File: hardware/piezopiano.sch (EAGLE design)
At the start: 82 parts, among them J1 CON2, J4 JST-PH-2-SMT-SE, Q1 DMN3404L, Q2 DMN3404L, Q3 DMN3404L, Q4 DMN3404L, Q5 DMN3404L, Q6 DMN3404L, Q7 DMN3404L, Q8 DMN3404L, U1 ATMEGA4809, U2 CH340E_MSOP10, U3 TP4333

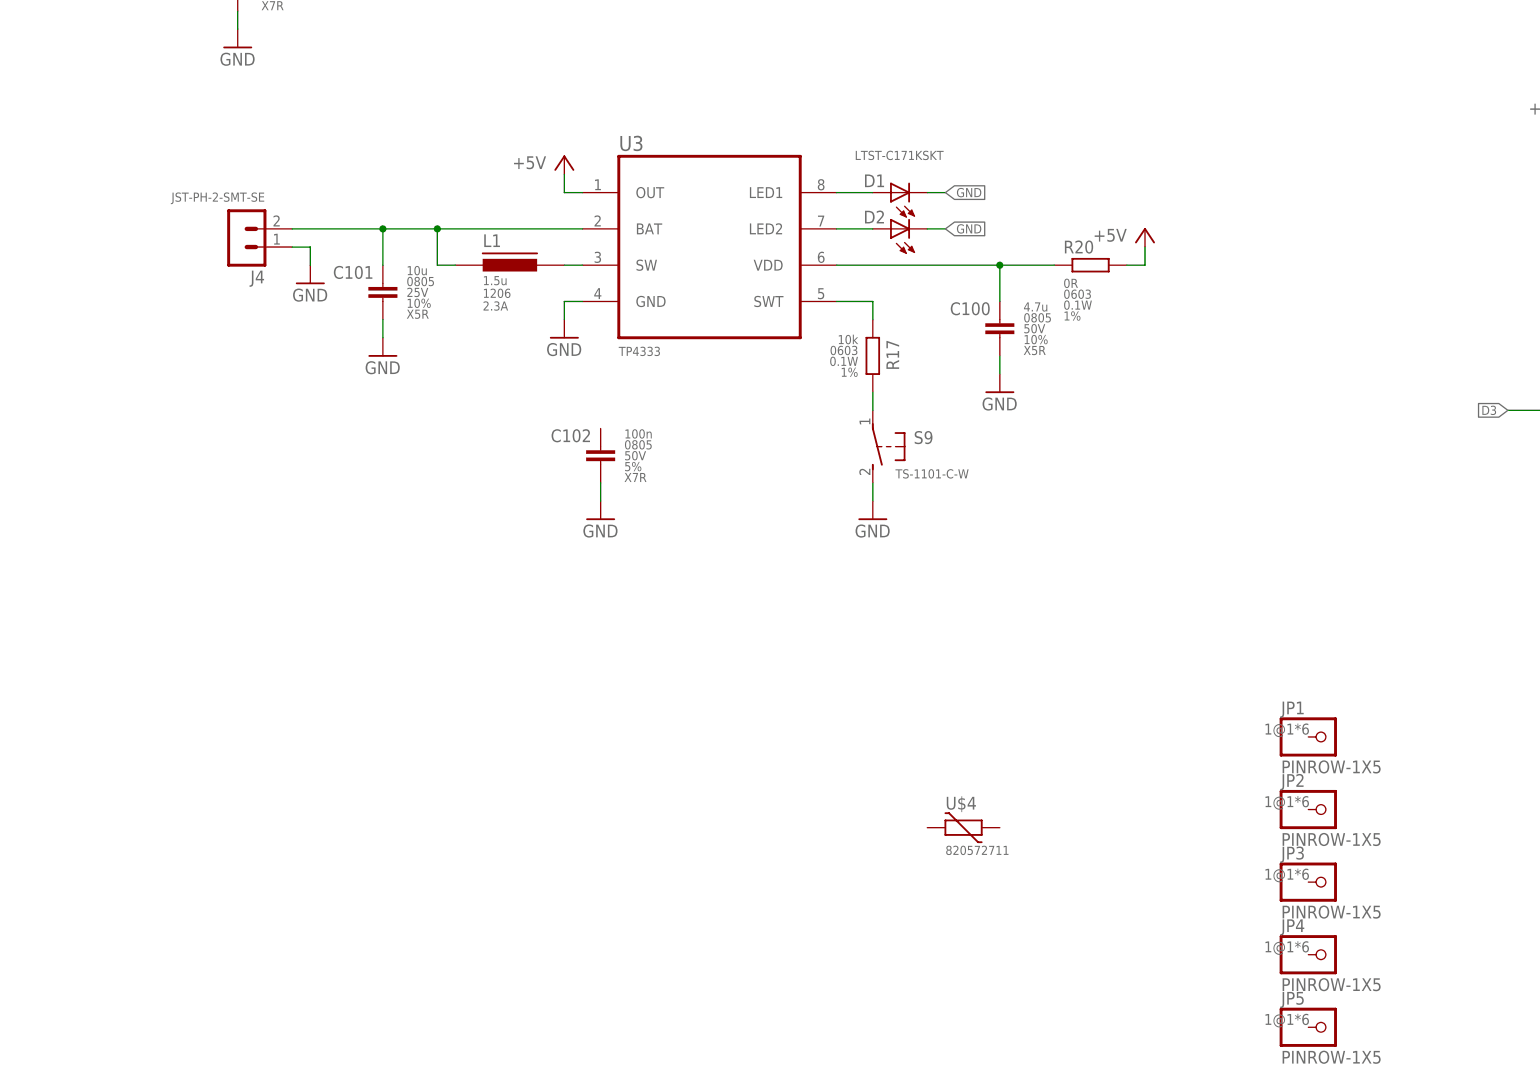
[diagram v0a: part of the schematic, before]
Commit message: Created different branch for battery support, deleted battery parts
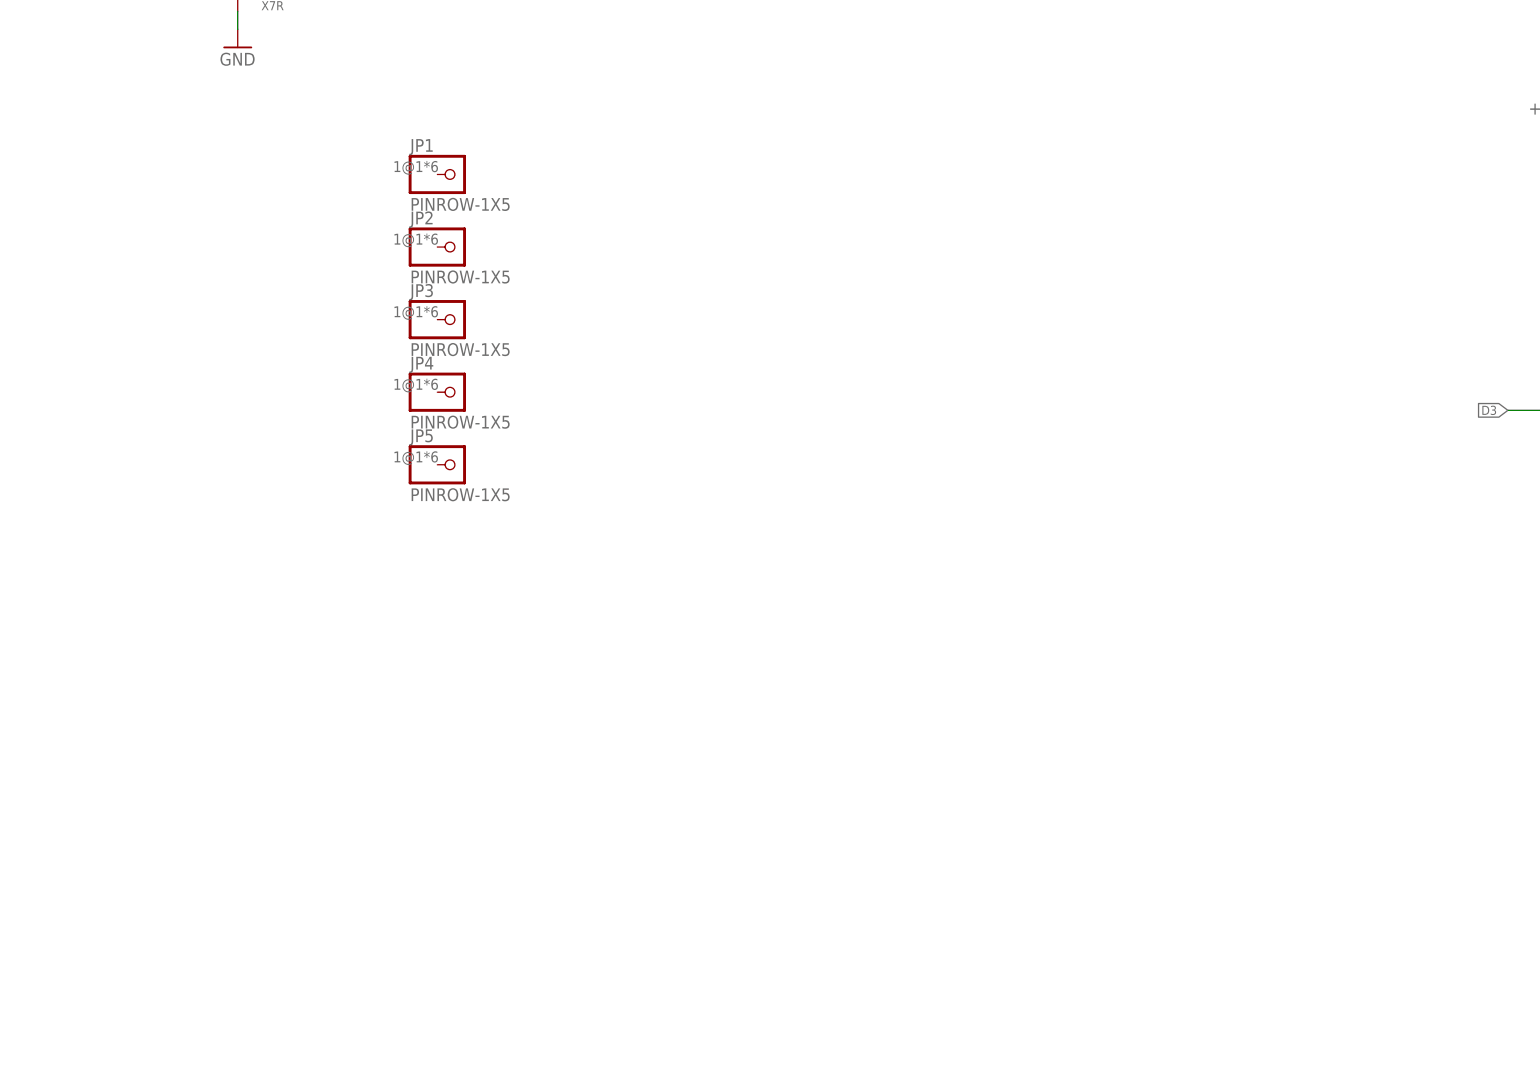
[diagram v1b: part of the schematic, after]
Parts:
- removed C100: 4.7u, zaan-Capacitors:4.7UF-0805-50V-10%
- removed C101: 10u, zaan-Capacitors:10UF-0805-25V-10%
- removed C102: 100n, zaan-Capacitors:100NF-0805-50V-5%
- removed D1, D2: LTST-C171KSKT, zaan-Optoelectronics:LTST-C171KSKT
- removed J4: JST-PH-2-SMT-SE, zaan-Connectors:JST-PH-2-SMT-SE
- removed L1: 1.5u, zaan-Inductors:WE-LQS-L3015-1.5U
- removed R17: 10k, zaan-Resistors:10KOHM-0603-1/10W-1%
- removed R20: 0R, zaan-Resistors:0OHM-0603-1/10W-1%
- removed S9: TS-1101-C-W, zaan-Electromechanical:TS-1101-C-W
- removed U$4: 820572711, zaan-No-Category:820572711
- removed U3: TP4333, zaan-IC-Power:TP4333
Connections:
- removed net N$17: C100.1, R20.1, U3.VDD
- removed net N$21: C101.1, J4.2, L1.1, U3.BAT
- removed net N$22: L1.2, U3.SW
- removed net N$23: R17.1, U3.SWT
- removed net N$24: R17.2, S9.P
- removed net N$25: D1.A, U3.LED1
- removed net N$26: D2.A, U3.LED2
- net +5V: no longer R20.2, U3.OUT
- net GND: no longer C100.2, C101.2, C102.2, D1.C, D2.C, J4.1, S9.S, U3.GND
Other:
- moved on the sheet: JP1, JP2, JP3, JP4, JP5

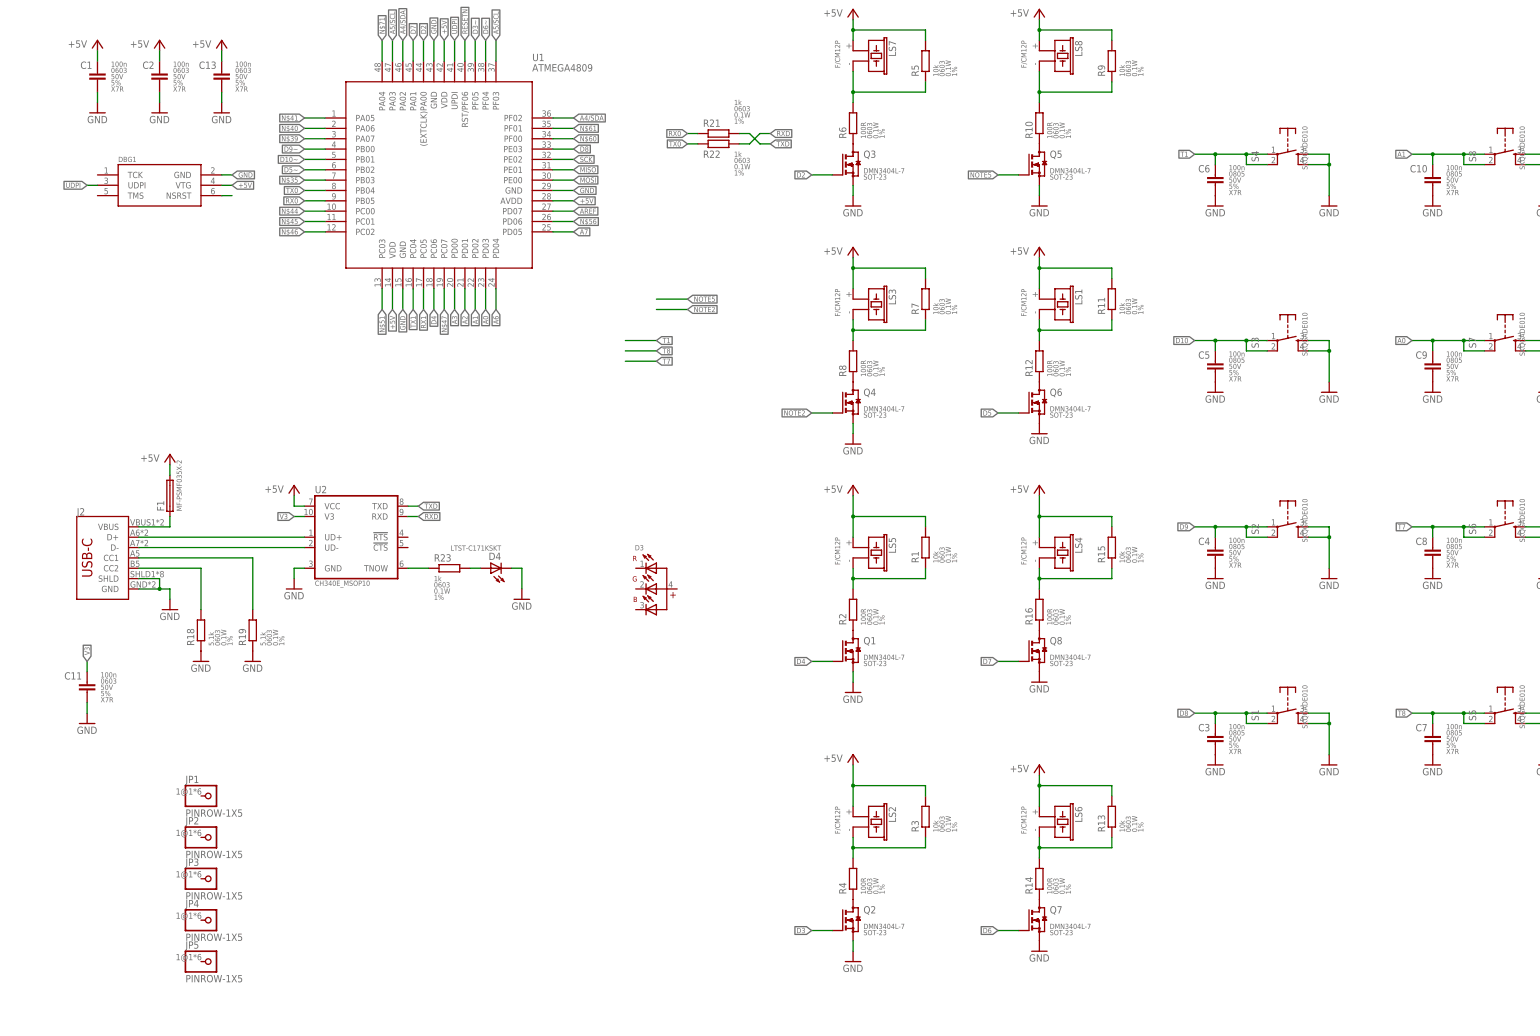
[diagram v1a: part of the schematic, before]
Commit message: Added QWIIC connector
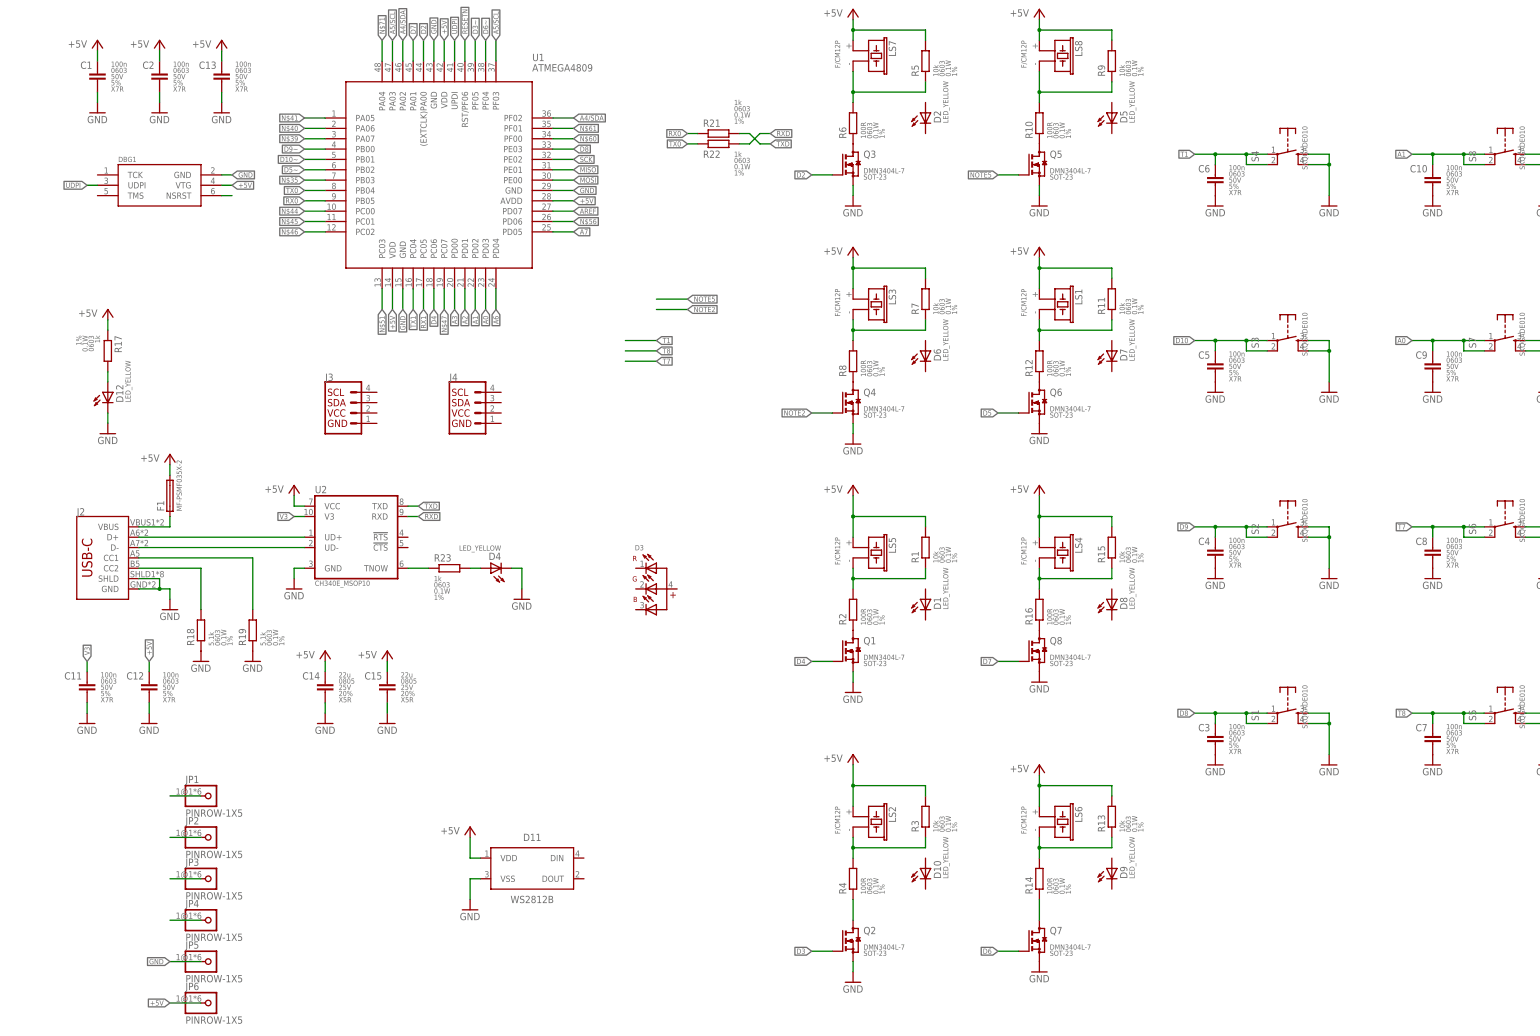
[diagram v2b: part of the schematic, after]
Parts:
- added C12: 100n, zaan-Capacitors:100NF-0603-50V-5%
- added C14, C15: 22u, zaan-Capacitors:22UF-0805-25V-20%
- added D1, D10, D12, D2, D5, D6, D7, D8, D9: LED_YELLOW, zaan-Optoelectronics:CHIP-FLAT-Y_0603-0.55MM
- added D11: WS2812B, zaan-Optoelectronics:WS2812B
- added J3, J4: (no value), zaan-Connectors:QWIIC_CONNECTORJS-1MM
- added JP6: PINROW-1X5, zaan-No-Category:PINROW-1X5
- added R17: 1k, zaan-Resistors:1KOHM-0603-1/10W-1%
- C10, C3, C4, C5, C6, C7, C8, C9: device zaan-Capacitors:100NF-0805-50V-5% -> zaan-Capacitors:100NF-0603-50V-5%
- D4: value LTST-C171KSKT -> LED_YELLOW; device zaan-Optoelectronics:LTST-C171KSKT -> zaan-Optoelectronics:CHIP-FLAT-Y_0603-0.55MM
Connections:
- new net N$22: JP4.1
- new net N$23: JP3.1
- new net N$24: JP2.1
- new net N$25: JP1.1
- new net N$8: D12.A, R17.2
- net +5V: now also C12.1, C14.1, C15.1, D11.VDD, JP6.1, R17.1
- net GND: now also C12.2, C14.2, C15.2, D11.VSS, D12.C, JP5.1
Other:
- moved on the sheet: Q2, Q7

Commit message: Routing and Placement changes
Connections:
- net N$22 renamed EXT_PH_04
- net N$23 renamed EXT_PH_03
- net N$24 renamed EXT_PH_02
- net N$25 renamed EXT_PH_01
- net N$35 renamed PB03
- net N$39 renamed PA07
- net N$40 renamed PA06
- net N$41 renamed PA05
- net N$44 renamed PC00
- net N$45 renamed PC01
- net N$46 renamed PC02
- net N$47 renamed PC07
- net N$51 renamed PC03
- net N$56 renamed PD06
- net N$60 renamed PF00
- net N$61 renamed PF01
- removed net D10: C5.1, S3.P, S3.P@1
- removed net N$28: DBG1.NSRST
- removed net N$71: U1.PA04
- removed net T1: C6.1, S4.P, S4.P@1
- removed net T8: C7.1, S5.P, S5.P@1
- new net PA04: C7.1, S5.P, S5.P@1, U1.PA04
- new net PF02: U1.PF02
- new net PF03: U1.PF03
- new net X: Q3.G
- new net Y: Q8.G
- net +5V: now also J3.VCC, J4.VCC
- net A4/SDA: now also J3.SDA, J4.SDA; no longer U1.PF02
- net A5/SCL: now also J3.SCL, J4.SCL; no longer U1.PF03
- net D2: now also C5.1, S3.P, S3.P@1; no longer Q3.G
- net D7: now also C6.1, S4.P, S4.P@1; no longer Q8.G
- net GND: now also J3.GND, J4.GND
